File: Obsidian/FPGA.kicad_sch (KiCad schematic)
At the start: 45 parts, among them Q1 BSS138LT1G, Q2 BSS138LT1G, SW2 SW_DIP_x01, U1 XC7A35T-CSG325, U28 24AA256UID-I_ST

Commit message: update with available components on LCSC
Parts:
- C123, C131, C132, C133, C141, C142: LCSC (none) -> C318563
- C124, C125, C126, C127, C134, C135, C136, C137, C143, C144, C145: LCSC (none) -> C85926
- C128, C129, C130, C138, C139, C140, C147, C148, C149: LCSC (none) -> C565524
- C227: LCSC (none) -> C110251
- LD3, LD4: LCSC (none) -> C5879295
- Q1, Q2: FT Rotation Offset (none) -> 180; LCSC (none) -> C82045
- R139, R140, R141, R182: LCSC (none) -> C25900
- R155, R156, R157, R158: LCSC (none) -> C60490
- R84: LCSC (none) -> C11702
- SW2: FT Rotation Offset (none) -> 0; LCSC (none) -> C7421519
- U1: FT Rotation Offset (none) -> 0; LCSC (none) -> C1521749
- U28: LCSC (none) -> C619605

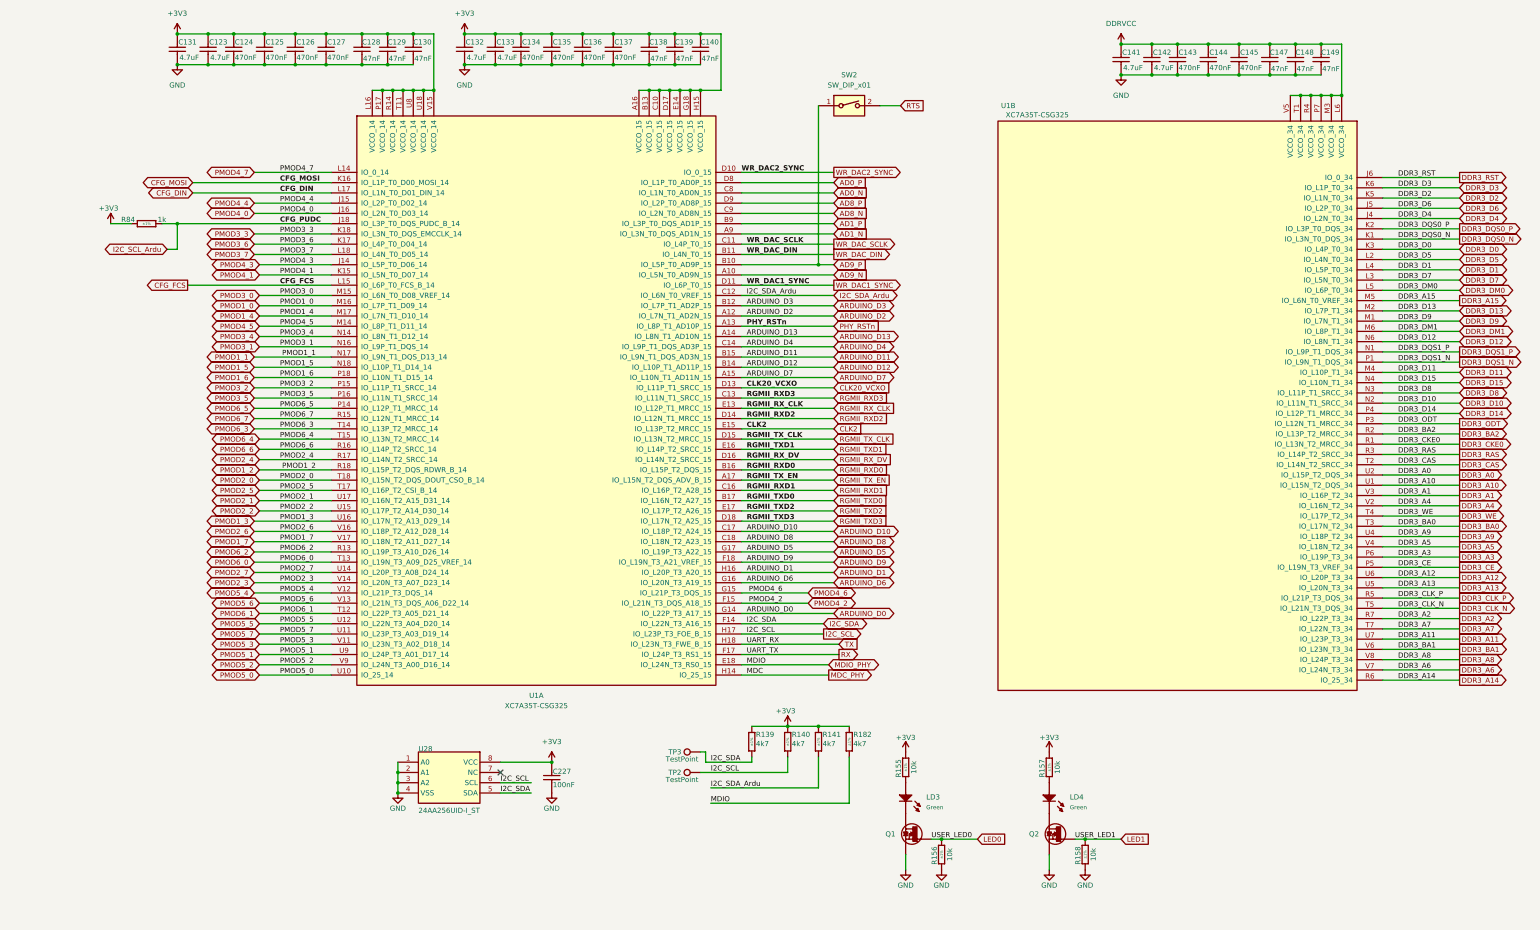
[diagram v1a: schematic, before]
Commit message: replacing global label with hierarchical label
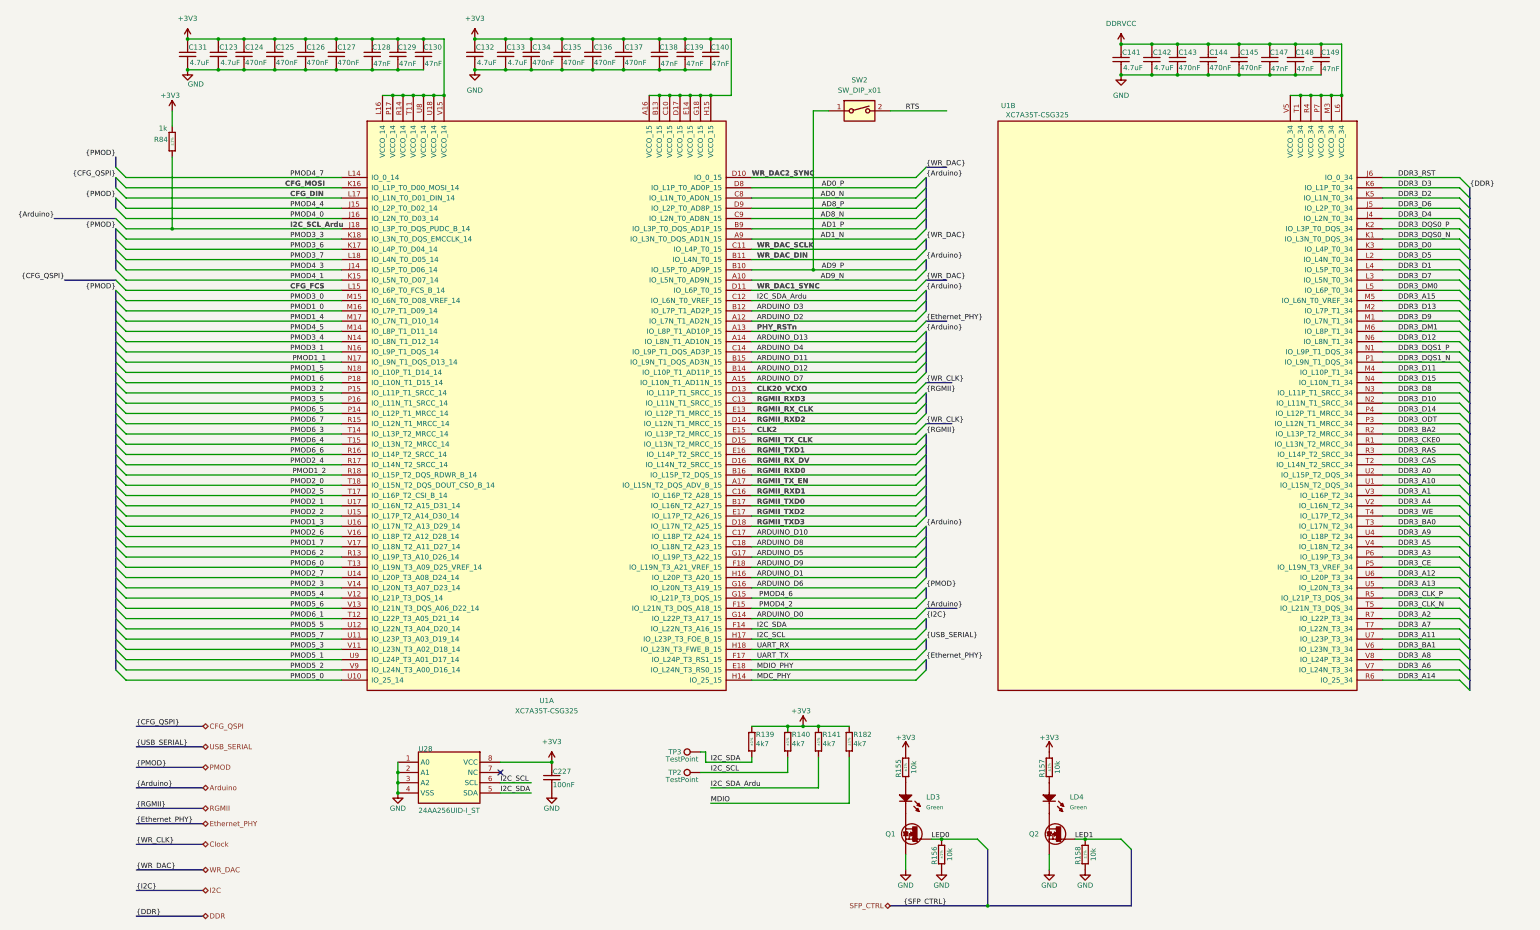
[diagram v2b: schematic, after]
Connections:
- net +3V3: now also R84.2; no longer R84.1
- net I2C_SCL_Ardu: now also R84.1; no longer R84.2
- net MDIO_PHY: no longer R182.1
- net RX renamed UART_TX
- net TX renamed UART_RX
- new net MDIO: R182.1
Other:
- moved on the sheet: C123, C124, C125, C126, C127, C128, C129, C130, C131, C132, C133, C134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

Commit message: Adding symbol library
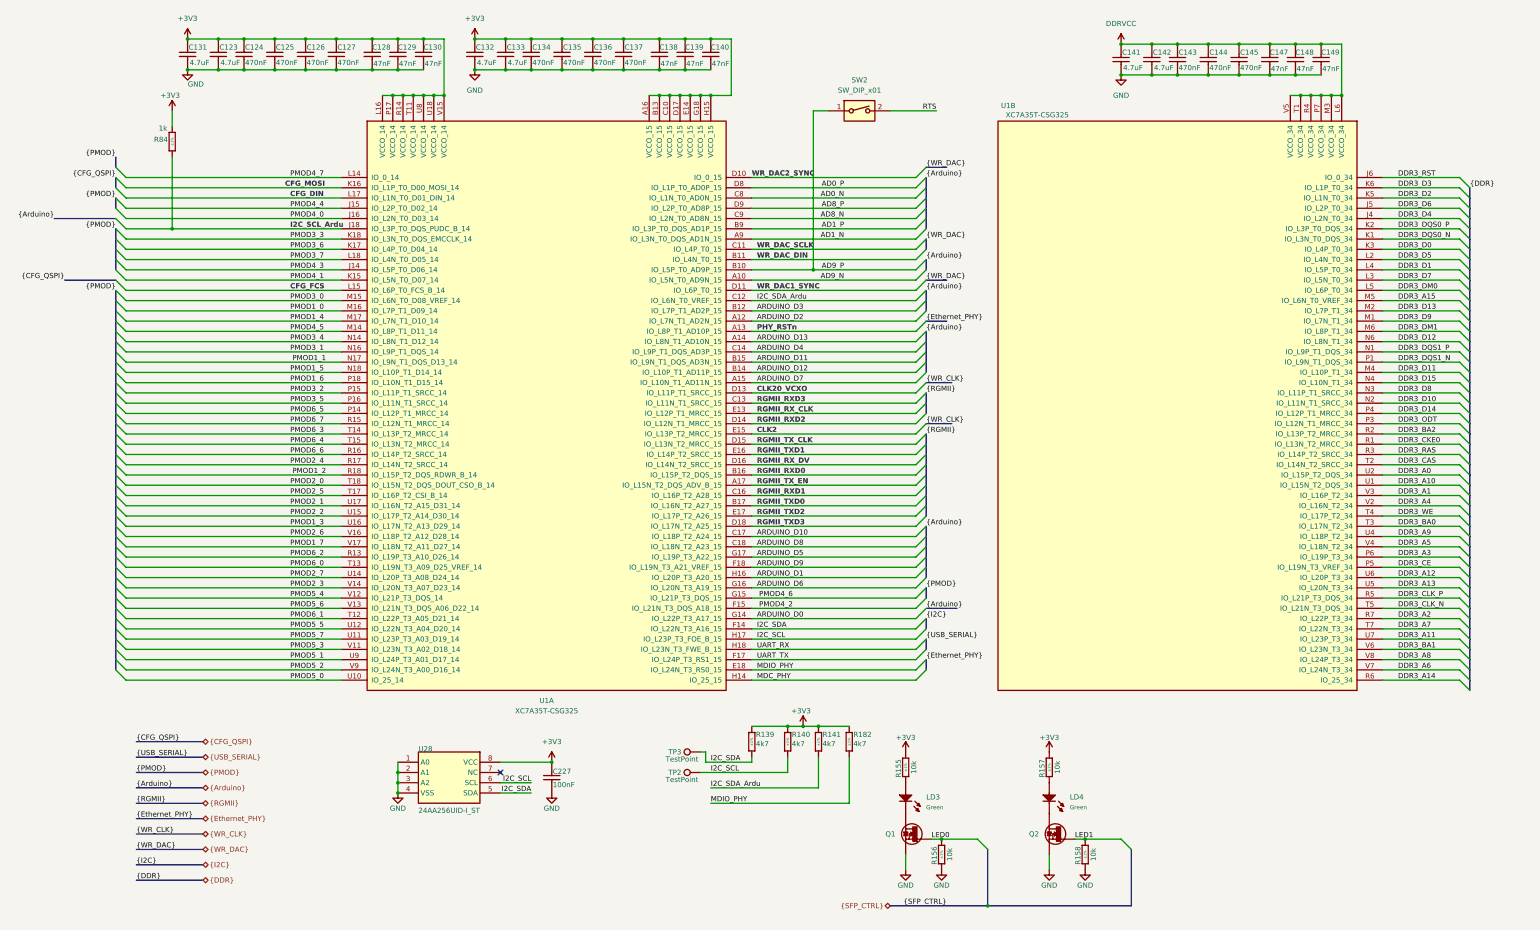
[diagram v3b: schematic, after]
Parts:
- C123, C131, C132, C133, C141, C142: symbol Capacitors SMD:CC0402_4.7UF_16V_20%_X5R -> Library_Symbol:CC0402_4.7UF_16V_20%_X5R
- C124, C125, C126, C127, C134, C135, C136, C137, C143, C144, C145: symbol Capacitors SMD:CC0201_470NF_4V_20%_X5R -> Library_Symbol:CC0201_470NF_4V_20%_X5R
- C128, C129, C130, C138, C139, C140, C147, C148, C149: symbol Capacitors SMD:CC0201_47NF_6.3V_10%_X5R -> Library_Symbol:CC0201_47NF_6.3V_10%_X5R
- C227: symbol Capacitors SMD:CC0402_100NF_50V_10%_X7R -> Library_Symbol:CC0402_100NF_50V_10%_X7R
- LD3, LD4: symbol LEDs & Displays:LED_KINGBRIGHT_KPH-1608CGCK -> Library_Symbol:LED_KINGBRIGHT_KPH-1608CGCK
- Q1, Q2: symbol Transistors:BSS138LT1G -> Library_Symbol:BSS138LT1G
- R139, R140, R141, R182: symbol Resistors SMD:R0402_4K7_1%_0.0625W_100PPM -> Library_Symbol:R0402_4K7_1%_0.0625W_100PPM
- R155, R156, R157, R158: symbol Resistors SMD:R0402_10K_1%_0.0625W_100PPM -> Library_Symbol:R0402_10K_1%_0.0625W_100PPM
- R84: symbol Resistors SMD:R0402_1K_1%_0.0625W_100PPM -> Library_Symbol:R0402_1K_1%_0.0625W_100PPM
- SW2: symbol Switch:SW_DIP_x01 -> Library_Symbol:SW_DIP_x01
- TP2, TP3: symbol Connector:TestPoint -> Library_Symbol:TestPoint
- U1: symbol FPGA_Xilinx_Artix7:XC7A35T-CSG325 -> Library_Symbol:XC7A35T-CSG325
- U28: symbol Sheet3-altium-import:root_0_24AA256UID-I_ST -> Library_Symbol:root_0_24AA256UID-I_ST
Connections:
- net MDIO is gone; now on net MDIO_PHY: R182.1

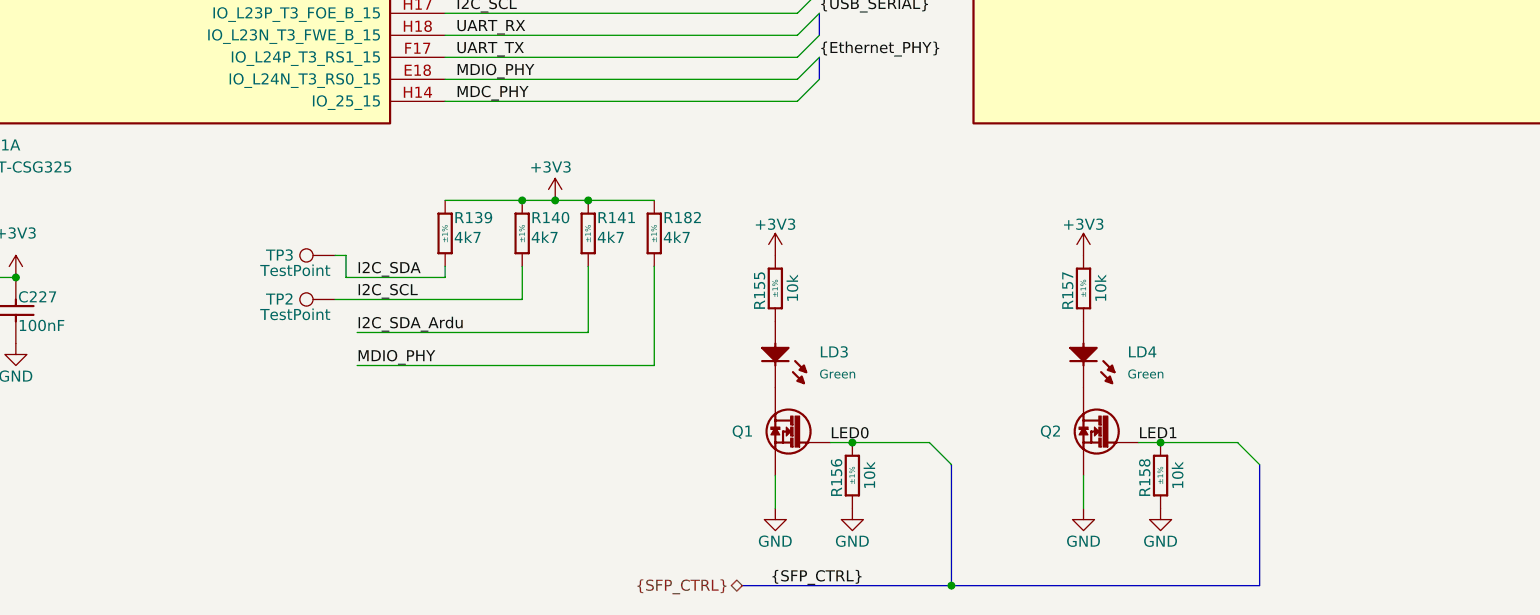
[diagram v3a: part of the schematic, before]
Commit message: Correct Schematic errors
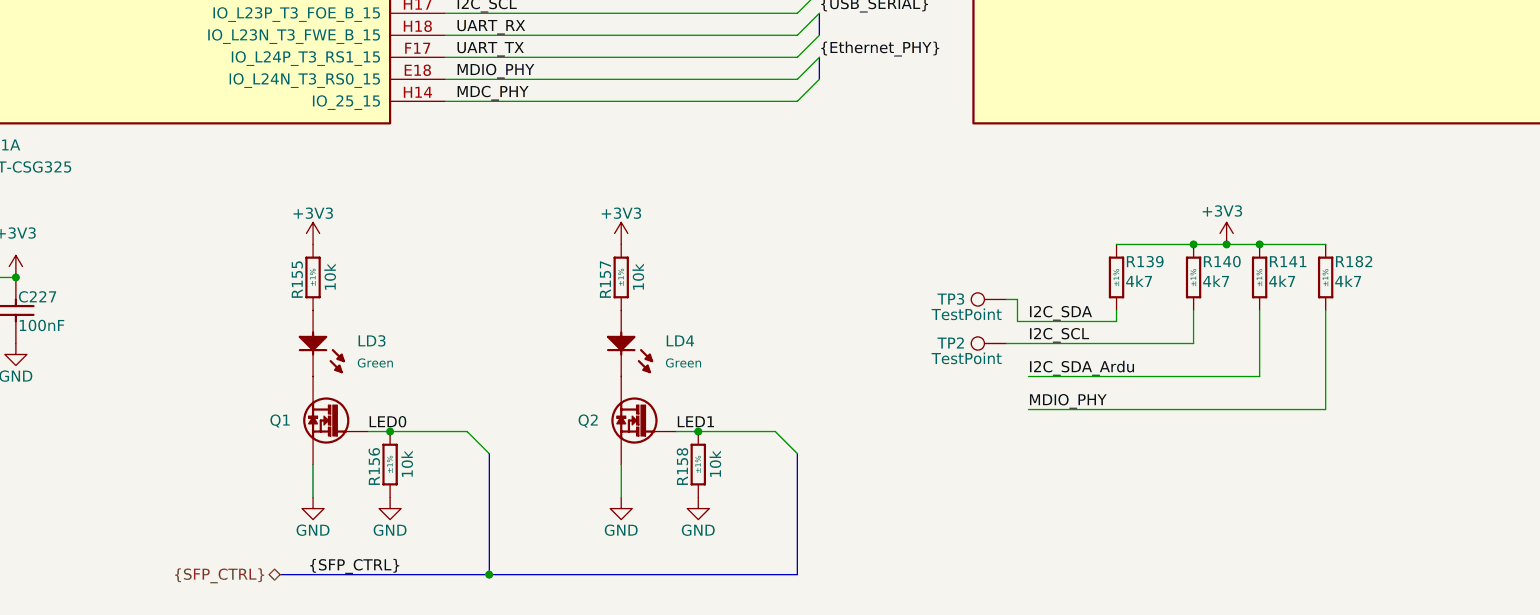
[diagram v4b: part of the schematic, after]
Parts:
- C123, C131, C132, C133, C141, C142, C227: footprint Capacitors SMD:CAPC1005X55N -> Footprint:CAPC1005X55N
- C124, C125, C126, C127, C128, C129, C130, C134, C135, C136, C137, C138, C139, C140, C143, C144, C145, C147, C148, C149: footprint Capacitors SMD:CAPC0603X33N -> Footprint:CAPC0603X33N
- LD3, LD4: footprint ICs And Semiconductors SMD:LED_KINGBRIGHT_KPH-1608CGCK -> Footprint:LED_KINGBRIGHT_KPH-1608CGCK
- Q1, Q2: footprint ICs And Semiconductors SMD:SOT95P240X110-3N -> Footprint:SOT95P240X110-3N
- R139, R140, R141, R155, R156, R157, R158, R182, R84: footprint Resistors SMD:RESC1005X40N -> Footprint:RESC1005X40N
- SW2: footprint Switches:SW_OMRON_A6SN-1101 -> Footprint:SW_OMRON_A6SN-1101
- U1: footprint Package_BGA:Xilinx_CSG325 -> Footprint:Xilinx_CSG325
- U28: footprint SOP65P640X120-8N -> Footprint:SOP65P640X120-8N
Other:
- moved on the sheet: LD3, LD4, Q1, Q2, R139, R140, R141, R155, R156, R157, R158, R182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

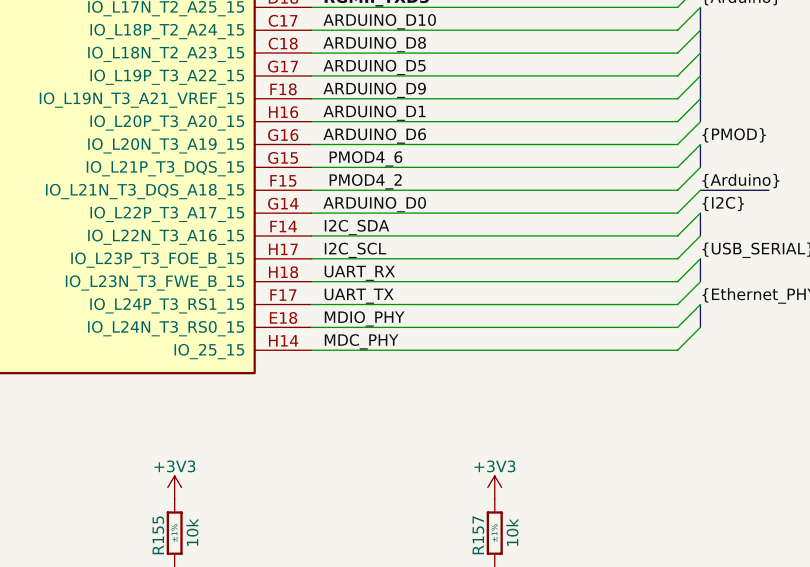
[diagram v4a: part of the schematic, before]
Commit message: correcting mismatch in TX/RX of UART
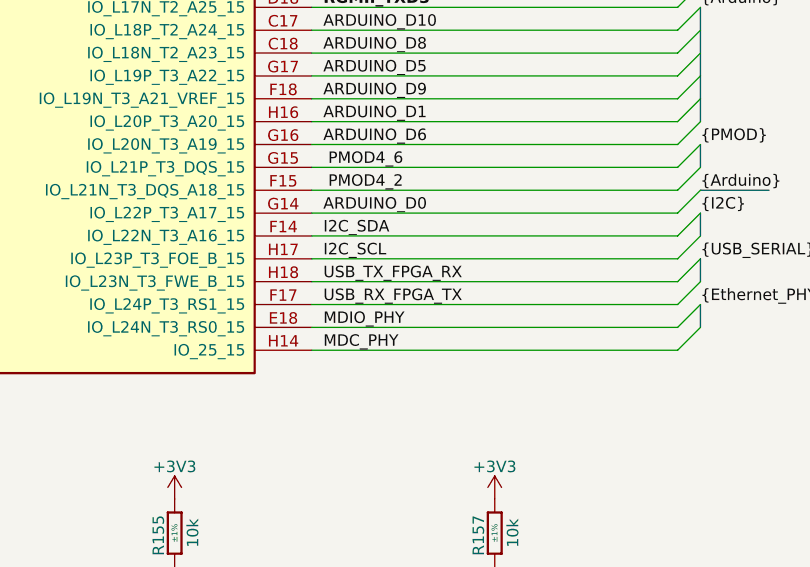
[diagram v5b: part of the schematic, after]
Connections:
- net UART_RX renamed USB_TX_FPGA_RX
- net UART_TX renamed USB_RX_FPGA_TX
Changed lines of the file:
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@@
 		)
 	)
-	(label "UART_TX"
+	(label "USB_RX_FPGA_TX"
 		(at 195.58 207.01 0)
 		(effects
@@
 		)
 	)
-	(label "UART_RX"
+	(label "USB_TX_FPGA_RX"
 		(at 195.58 204.47 0)
 		(effects
